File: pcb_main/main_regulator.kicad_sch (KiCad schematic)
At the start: 29 parts, among them IC301 OPA277, IC302 OPA277, Q301 BD249C, Q302 BD139, Q303 BD249C, Q304 BC557, Q305 BD139, Q306 BD249C, Q307 BD139

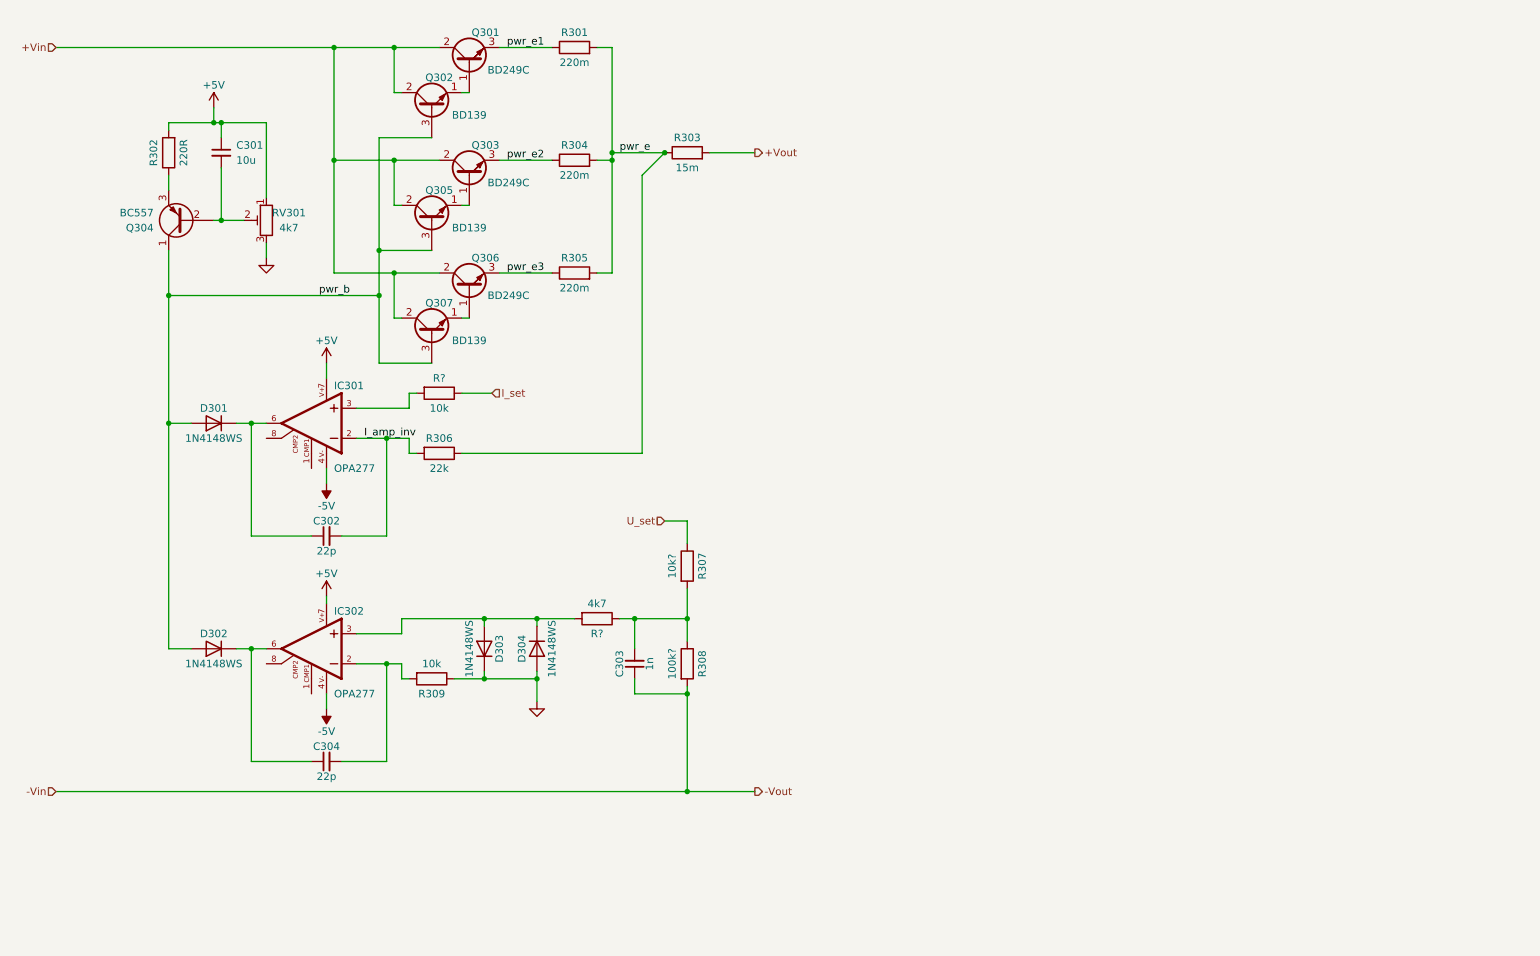
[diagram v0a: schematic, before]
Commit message: power tracks routed
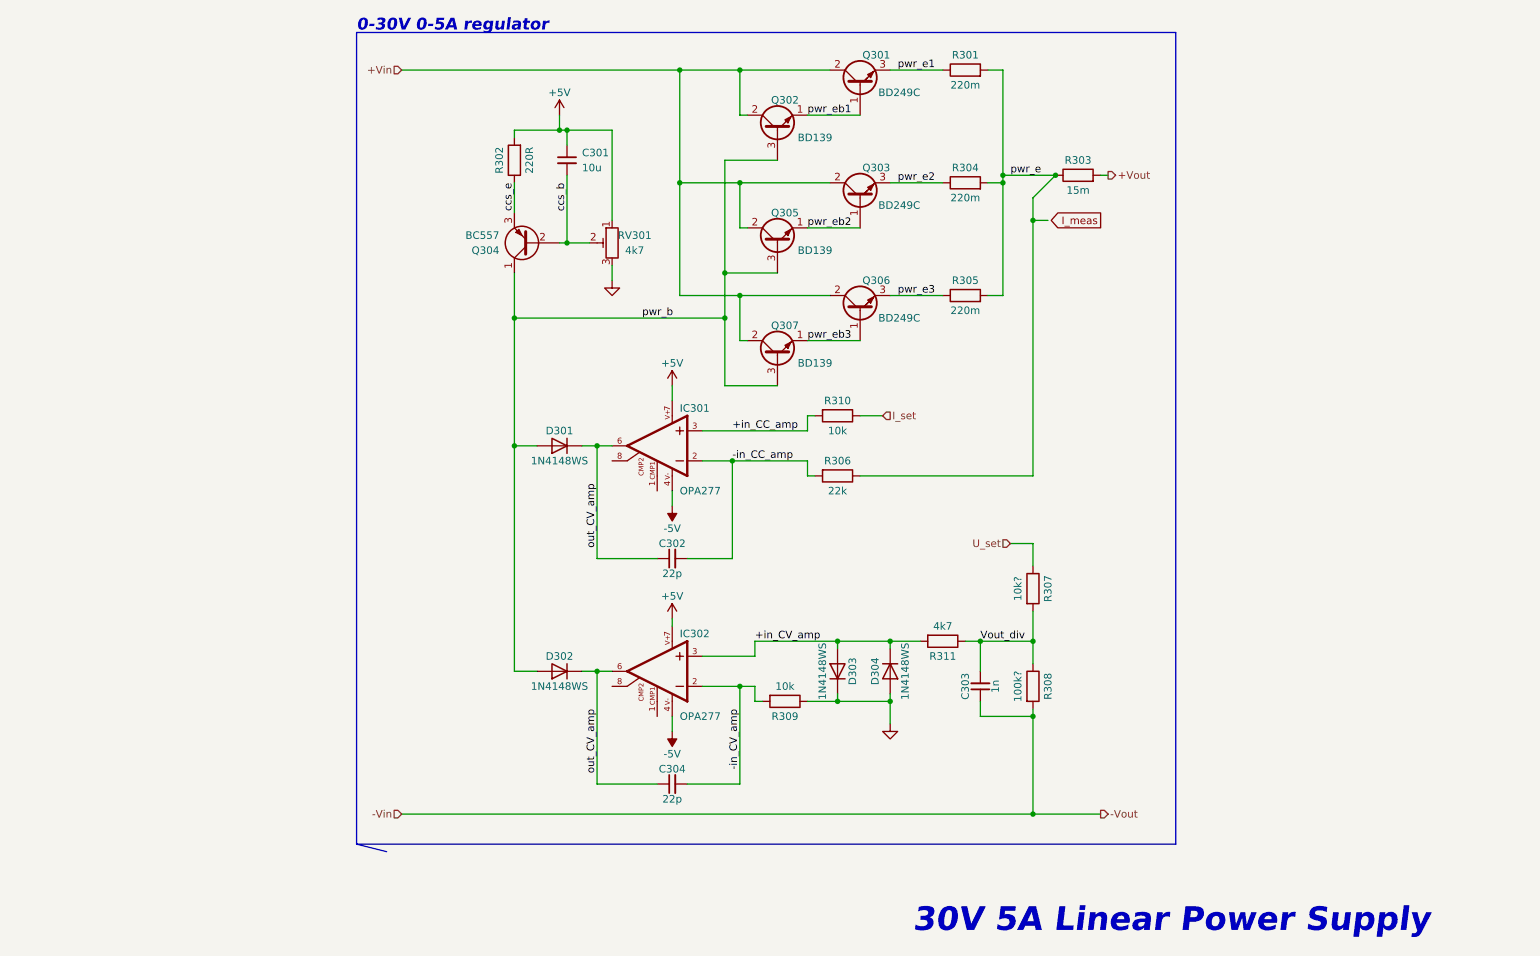
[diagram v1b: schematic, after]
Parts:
- RV301: footprint Potentiometer_THT:Potentiometer_Vishay_T73YP_Vertical -> Potentiometer_THT:Potentiometer_Piher_PT-6-V_Vertical
- gave numbers to parts that had none: 2
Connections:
- net ccs_b: now reaches C301.2, Q304.2 (B), RV301.2
- net out_CV_amp: now reaches C302.1, D301.1 (K), IC301.6
- net out_CV_amp: now also C304.1, D302.1 (K), IC302.6
- net Vout_div: now reaches C303.2, R307.2, R308.1, R311.1
- net ccs_e: now reaches Q304.3 (E), R302.1
- net pwr_eb1: now reaches Q301.1 (B), Q302.1 (E)
- net +in_CC_amp: now reaches IC301.3, R310.2
- net -in_CV_amp: now reaches C304.2, IC302.2, R309.2
- net pwr_eb2: now reaches Q303.1 (B), Q305.1 (E)
- net +in_CV_amp: now reaches D303.2 (A), D304.1 (K), IC302.3, R311.2
- net pwr_eb3: now reaches Q306.1 (B), Q307.1 (E)
- net I_amp_inv renamed -in_CC_amp
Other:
- note added: "0-30V 0-5A regulator"
- note added: "30V 5A Linear Power Supply"
- company: (none) -> Dominik Workshop
- title: (none) -> Main linear regulator
- moved on the sheet: C301, C302, C303, C304, D301, D302, D303, D304, IC301, IC302, Q301, Q302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

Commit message: most layout done
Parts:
- C302, C304: footprint Resistor_SMD:R_0603_1608Metric -> Capacitor_SMD:C_0603_1608Metric
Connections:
- net pwr_e is gone; now on net I_meas: R301.2, R303.1, R304.2, R305.2, R306.1
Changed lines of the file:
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@@
     (stroke (width 0) (type default) (color 0 0 0 0))
   )
-  (wire (pts (xy 201.93 55.88) (xy 204.47 55.88))
+  (wire (pts (xy 201.93 55.88) (xy 207.01 55.88))
     (stroke (width 0) (type default) (color 0 0 0 0))
   )
@@
     (effects (font (size 1.27 1.27)) (justify left bottom))
   )
-  (label "pwr_e" (at 198.12 48.26 0)
-    (effects (font (size 1.27 1.27)) (justify left bottom))
-  )
   (label "+in_CC_amp" (at 151.13 91.44 0)
     (effects (font (size 1.27 1.27)) (justify left bottom))
@@
     (effects (font (size 1.27 1.27)) (justify left bottom))
   )
-  (global_label "I_meas" (shape output) (at 213.36 55.88 180) (fields_autoplaced)
-    (effects (font (size 1.27 1.27)) (justify right))
-    (property "Intersheet References" "${INTERSHEET_REFS}" (id 0) (at 204.4155 55.8006 0)
-      (effects (font (size 1.27 1.27)) (justify right) hide)
+  (global_label "I_meas" (shape output) (at 207.01 55.88 0) (fields_autoplaced)
+    (effects (font (size 1.27 1.27)) (justify left))
+    (property "Intersheet References" "${INTERSHEET_REFS}" (id 0) (at 215.9545 55.9594 0)
+      (effects (font (size 1.27 1.27)) (justify left) hide)
     )
   )
@@
     (property "Reference" "C302" (id 0) (at 140.97 110.49 90))
     (property "Value" "22p" (id 1) (at 140.97 115.57 90))
-    (property "Footprint" "Resistor_SMD:R_0603_1608Metric" (id 2) (at 140.97 113.03 0)
+    (property "Footprint" "Capacitor_SMD:C_0603_1608Metric" (id 2) (at 140.97 113.03 0)
       (effects (font (size 1.27 1.27)) hide)
     )
@@
     (property "Reference" "C304" (id 0) (at 140.97 148.59 90))
     (property "Value" "22p" (id 1) (at 140.97 153.67 90))
-    (property "Footprint" "Resistor_SMD:R_0603_1608Metric" (id 2) (at 140.97 151.13 0)
-      (effects (font (size 1.27 1.27)) hide)
-    )
+    (property "Footprint" "Capacitor_SMD:C_0603_1608Metric" (id 2) (at 140.97 151.13 0)
+      (effects (font (size 1.27 1.27)) hide)
+    )
